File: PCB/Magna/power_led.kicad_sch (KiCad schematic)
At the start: 14 parts

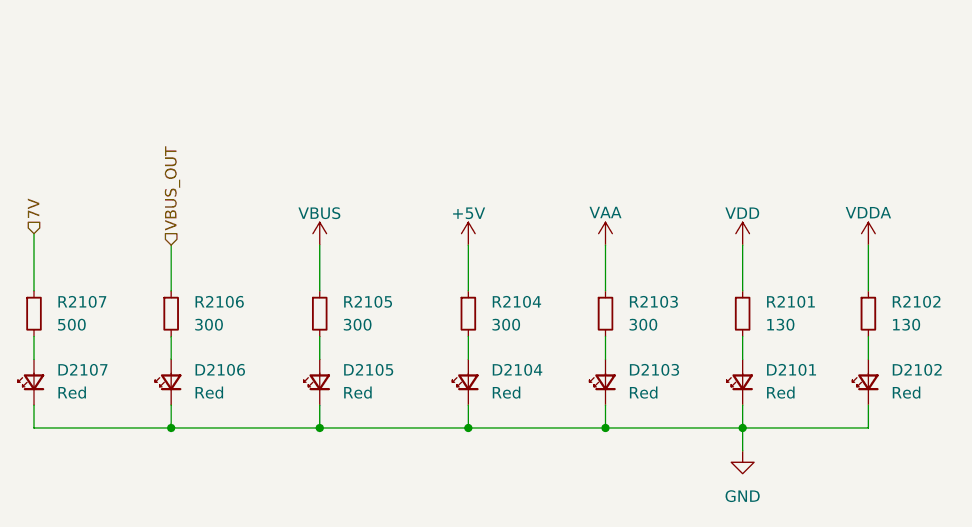
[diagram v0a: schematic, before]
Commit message: Update capacitors to parts in JLC library
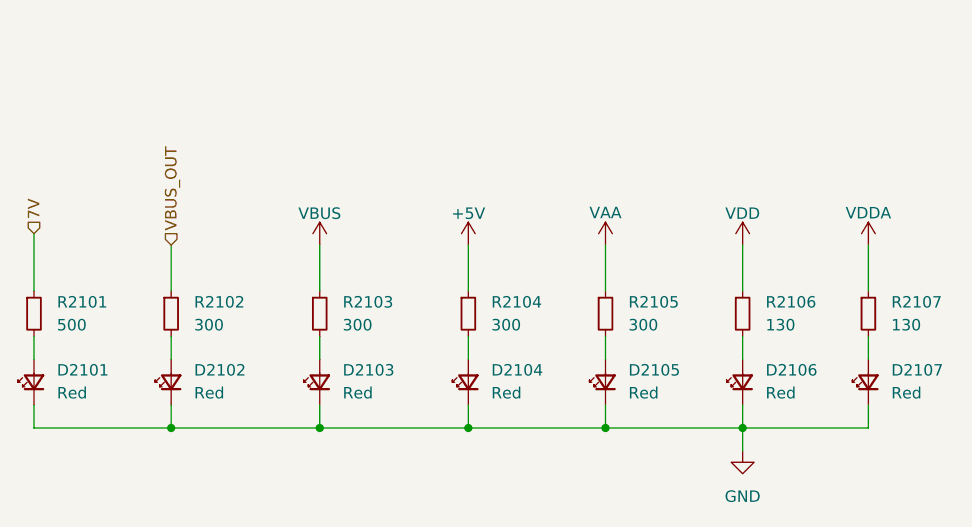
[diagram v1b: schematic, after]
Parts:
- renumbered D2107 to D2101, D2106 to D2102, D2105 to D2103, D2103 to D2105, D2101 to D2106, D2102 to D2107, R2107 to R2101, R2106 to R2102, R2105 to R2103, R2103 to R2105, R2101 to R2106, R2102 to R2107

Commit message: Select parts for all components
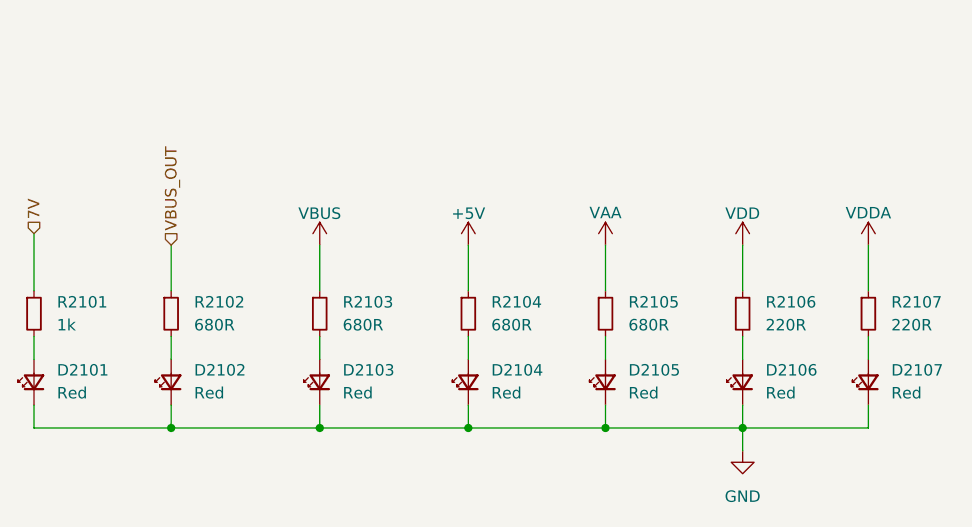
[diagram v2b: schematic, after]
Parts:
- D2101, D2102, D2103, D2104, D2105, D2106, D2107: footprint (none) -> Diode_SMD:D_0805_2012Metric_Pad1.15x1.40mm_HandSolder; LCSC (none) -> C84256
- R2101: value 500 -> 1k; footprint (none) -> Resistor_SMD:R_0805_2012Metric_Pad1.20x1.40mm_HandSolder; LCSC (none) -> C17513
- R2102, R2103, R2104, R2105: value 300 -> 680R; footprint (none) -> Resistor_SMD:R_0805_2012Metric_Pad1.20x1.40mm_HandSolder; LCSC (none) -> C865612
- R2106, R2107: value 130 -> 220R; footprint (none) -> Resistor_SMD:R_0805_2012Metric_Pad1.20x1.40mm_HandSolder; LCSC (none) -> C17557
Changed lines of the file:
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@@
       (effects (font (size 1.27 1.27)) (justify left))
     )
-    (property "Value" "300" (at 97.79 63.5 0)
-      (effects (font (size 1.27 1.27)) (justify left))
-    )
-    (property "Footprint" "" (at 95.25 62.23 0)
+    (property "Value" "680R" (at 97.79 63.5 0)
+      (effects (font (size 1.27 1.27)) (justify left))
+    )
+    (property "Footprint" "Resistor_SMD:R_0805_2012Metric_Pad1.20x1.40mm_HandSolder" (at 95.25 62.23 0)
       (effects (font (size 1.27 1.27)) hide)
     )
@@
       (effects (font (size 1.27 1.27)) hide)
     )
+    (property "LCSC" "C865612" (at 95.25 62.23 0)
+      (effects (font (size 1.27 1.27)) hide)
+    )
     (pin "1")
     (pin "2")
@@
       (effects (font (size 1.27 1.27)) (justify right))
     )
-    (property "Footprint" "" (at 111.76 69.85 90)
+    (property "Footprint" "Diode_SMD:D_0805_2012Metric_Pad1.15x1.40mm_HandSolder" (at 111.76 69.85 90)
       (effects (font (size 1.27 1.27)) hide)
     )
     (property "Datasheet" "~" (at 111.76 69.85 90)
+      (effects (font (size 1.27 1.27)) hide)
+    )
+    (property "LCSC" "C84256" (at 111.76 69.85 0)
       (effects (font (size 1.27 1.27)) hide)
     )
@@
       (effects (font (size 1.27 1.27)) (justify right))
     )
-    (property "Footprint" "" (at 78.74 69.85 90)
+    (property "Footprint" "Diode_SMD:D_0805_2012Metric_Pad1.15x1.40mm_HandSolder" (at 78.74 69.85 90)
       (effects (font (size 1.27 1.27)) hide)
     )
@@
       (effects (font (size 1.27 1.27)) hide)
     )
+    (property "LCSC" "C84256" (at 78.74 69.85 0)
+      (effects (font (size 1.27 1.27)) hide)
+    )
     (pin "2")
     (pin "1")
@@
       (effects (font (size 1.27 1.27)) (justify right))
     )
-    (property "Footprint" "" (at 95.25 69.85 90)
+    (property "Footprint" "Diode_SMD:D_0805_2012Metric_Pad1.15x1.40mm_HandSolder" (at 95.25 69.85 90)
       (effects (font (size 1.27 1.27)) hide)
     )
@@
       (effects (font (size 1.27 1.27)) hide)
     )
+    (property "LCSC" "C84256" (at 95.25 69.85 0)
+      (effects (font (size 1.27 1.27)) hide)
+    )
     (pin "2")
     (pin "1")
@@
       (effects (font (size 1.27 1.27)) (justify left))
     )
-    (property "Value" "300" (at 114.3 63.5 0)
-      (effects (font (size 1.27 1.27)) (justify left))
-    )
-    (property "Footprint" "" (at 111.76 62.23 0)
+    (property "Value" "680R" (at 114.3 63.5 0)
+      (effects (font (size 1.27 1.27)) (justify left))
+    )
+    (property "Footprint" "Resistor_SMD:R_0805_2012Metric_Pad1.20x1.40mm_HandSolder" (at 111.76 62.23 0)
       (effects (font (size 1.27 1.27)) hide)
     )
@@
       (effects (font (size 1.27 1.27)) hide)
     )
+    (property "LCSC" "C865612" (at 111.76 62.23 0)
+      (effects (font (size 1.27 1.27)) hide)
+    )
     (pin "1")
     (pin "2")
@@
       (effects (font (size 1.27 1.27)) (justify right))
     )
-    (property "Footprint" "" (at 142.24 69.85 90)
+    (property "Footprint" "Diode_SMD:D_0805_2012Metric_Pad1.15x1.40mm_HandSolder" (at 142.24 69.85 90)
       (effects (font (size 1.27 1.27)) hide)
     )
@@
       (effects (font (size 1.27 1.27)) hide)
     )
+    (property "LCSC" "C84256" (at 142.24 69.85 0)
+      (effects (font (size 1.27 1.27)) hide)
+    )
     (pin "2")
     (pin "1")
@@
       (effects (font (size 1.27 1.27)) (justify left))
     )
-    (property "Value" "300" (at 129.54 63.5 0)
-      (effects (font (size 1.27 1.27)) (justify left))
-    )
-    (property "Footprint" "" (at 127 62.23 0)
+    (property "Value" "680R" (at 129.54 63.5 0)
+      (effects (font (size 1.27 1.27)) (justify left))
+    )
+    (property "Footprint" "Resistor_SMD:R_0805_2012Metric_Pad1.20x1.40mm_HandSolder" (at 127 62.23 0)
       (effects (font (size 1.27 1.27)) hide)
     )
@@
       (effects (font (size 1.27 1.27)) hide)
     )
+    (property "LCSC" "C865612" (at 127 62.23 0)
+      (effects (font (size 1.27 1.27)) hide)
+    )
     (pin "1")
     (pin "2")
@@
       (effects (font (size 1.27 1.27)) (justify left))
     )
-    (property "Value" "300" (at 81.28 63.5 0)
-      (effects (font (size 1.27 1.27)) (justify left))
-    )
-    (property "Footprint" "" (at 78.74 62.23 0)
+    (property "Value" "680R" (at 81.28 63.5 0)
+      (effects (font (size 1.27 1.27)) (justify left))
+    )
+    (property "Footprint" "Resistor_SMD:R_0805_2012Metric_Pad1.20x1.40mm_HandSolder" (at 78.74 62.23 0)
       (effects (font (size 1.27 1.27)) hide)
     )
     (property "Datasheet" "~" (at 78.74 62.23 0)
+      (effects (font (size 1.27 1.27)) hide)
+    )
+    (property "LCSC" "C865612" (at 78.74 62.23 0)
       (effects (font (size 1.27 1.27)) hide)
     )
@@
       (effects (font (size 1.27 1.27)) (justify left))
     )
-    (property "Value" "130" (at 158.75 63.5 0)
-      (effects (font (size 1.27 1.27)) (justify left))
-    )
-    (property "Footprint" "" (at 156.21 62.23 0)
+    (property "Value" "220R" (at 158.75 63.5 0)
+      (effects (font (size 1.27 1.27)) (justify left))
+    )
+    (property "Footprint" "Resistor_SMD:R_0805_2012Metric_Pad1.20x1.40mm_HandSolder" (at 156.21 62.23 0)
       (effects (font (size 1.27 1.27)) hide)
     )
@@
       (effects (font (size 1.27 1.27)) hide)
     )
+    (property "LCSC" "C17557" (at 156.21 62.23 0)
+      (effects (font (size 1.27 1.27)) hide)
+    )
     (pin "1")
     (pin "2")
@@
       (effects (font (size 1.27 1.27)) (justify right))
     )
-    (property "Footprint" "" (at 127 69.85 90)
+    (property "Footprint" "Diode_SMD:D_0805_2012Metric_Pad1.15x1.40mm_HandSolder" (at 127 69.85 90)
       (effects (font (size 1.27 1.27)) hide)
     )
@@
       (effects (font (size 1.27 1.27)) hide)
     )
+    (property "LCSC" "C84256" (at 127 69.85 0)
+      (effects (font (size 1.27 1.27)) hide)
+    )
     (pin "2")
     (pin "1")
@@
       (effects (font (size 1.27 1.27)) (justify right))
     )
-    (property "Footprint" "" (at 63.5 69.85 90)
+    (property "Footprint" "Diode_SMD:D_0805_2012Metric_Pad1.15x1.40mm_HandSolder" (at 63.5 69.85 90)
       (effects (font (size 1.27 1.27)) hide)
     )
@@
       (effects (font (size 1.27 1.27)) hide)
     )
+    (property "LCSC" "C84256" (at 63.5 69.85 0)
+      (effects (font (size 1.27 1.27)) hide)
+    )
     (pin "2")
     (pin "1")
@@
       (effects (font (size 1.27 1.27)) (justify left))
     )
-    (property "Value" "500" (at 66.04 63.5 0)
-      (effects (font (size 1.27 1.27)) (justify left))
-    )
-    (property "Footprint" "" (at 63.5 62.23 0)
+    (property "Value" "1k" (at 66.04 63.5 0)
+      (effects (font (size 1.27 1.27)) (justify left))
+    )
+    (property "Footprint" "Resistor_SMD:R_0805_2012Metric_Pad1.20x1.40mm_HandSolder" (at 63.5 62.23 0)
       (effects (font (size 1.27 1.27)) hide)
     )
@@
       (effects (font (size 1.27 1.27)) hide)
     )
+    (property "LCSC" "C17513" (at 63.5 62.23 0)
+      (effects (font (size 1.27 1.27)) hide)
+    )
     (pin "1")
     (pin "2")
@@
       (effects (font (size 1.27 1.27)) (justify right))
     )
-    (property "Footprint" "" (at 156.21 69.85 90)
+    (property "Footprint" "Diode_SMD:D_0805_2012Metric_Pad1.15x1.40mm_HandSolder" (at 156.21 69.85 90)
       (effects (font (size 1.27 1.27)) hide)
     )
@@
       (effects (font (size 1.27 1.27)) hide)
     )
+    (property "LCSC" "C84256" (at 156.21 69.85 0)
+      (effects (font (size 1.27 1.27)) hide)
+    )
     (pin "2")
     (pin "1")
@@
       (effects (font (size 1.27 1.27)) (justify left))
     )
-    (property "Value" "130" (at 144.78 63.5 0)
-      (effects (font (size 1.27 1.27)) (justify left))
-    )
-    (property "Footprint" "" (at 142.24 62.23 0)
+    (property "Value" "220R" (at 144.78 63.5 0)
+      (effects (font (size 1.27 1.27)) (justify left))
+    )
+    (property "Footprint" "Resistor_SMD:R_0805_2012Metric_Pad1.20x1.40mm_HandSolder" (at 142.24 62.23 0)
       (effects (font (size 1.27 1.27)) hide)
     )
@@
       (effects (font (size 1.27 1.27)) hide)
     )
+    (property "LCSC" "C17557" (at 142.24 62.23 0)
+      (effects (font (size 1.27 1.27)) hide)
+    )

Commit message: Move VAA circuitry to Analogue daughterboard (#11)
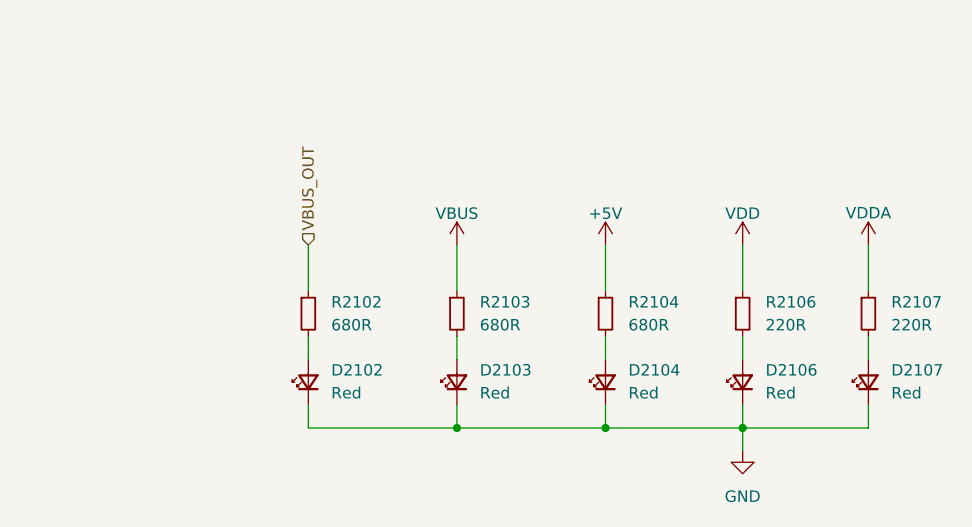
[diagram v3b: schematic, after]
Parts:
- removed D2101, D2105: Red, Diode_SMD:D_0805_2012Metric_Pad1.15x1.40mm_HandSolder, symbol Device:LED_Small
- removed R2101: 1k, Resistor_SMD:R_0805_2012Metric_Pad1.20x1.40mm_HandSolder, symbol Device:R_Small
- removed R2105: 680R, Resistor_SMD:R_0805_2012Metric_Pad1.20x1.40mm_HandSolder, symbol Device:R_Small
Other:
- moved on the sheet: D2102, D2103, D2104, R2102, R2103, R2104
